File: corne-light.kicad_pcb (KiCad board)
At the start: 2 copper layers, 279.5 x 91.4 mm, 112 parts, among them J1 MJ-4PP-9, J2 OLED, J3 Conn_01x02, J4 Conn_01x02, J6 MJ-4PP-9, J7 OLED, SW1 SW_PUSH, SW10 SW_PUSH, SW11 SW_PUSH, SW12 SW_PUSH, SW13 SW_PUSH, SW14 SW_PUSH, SW15 SW_PUSH, SW16 SW_PUSH, SW17 SW_PUSH, SW18 SW_PUSH, SW19 SW_PUSH, SW2 SW_PUSH, SW20 SW_PUSH, SW21 SW_PUSH, SW22 SW_PUSH, SW23 SW_PUSH, SW24 SW_PUSH, SW25 SW_PUSH, SW26 SW_PUSH, SW27 SW_PUSH, SW28 SW_PUSH, SW29 SW_PUSH, SW3 SW_PUSH, SW30 SW_PUSH, SW31 SW_PUSH, SW32 SW_PUSH, SW33 SW_PUSH, SW34 SW_PUSH, SW35 SW_PUSH, SW36 SW_PUSH, SW37 SW_PUSH, SW38 SW_PUSH, SW39 SW_PUSH, SW4 SW_PUSH, SW40 SW_PUSH, SW41 SW_PUSH, SW42 SW_PUSH, SW44 SW_Slide_DPDT, SW45 SW_Slide_DPDT, SW5 SW_PUSH, SW6 SW_PUSH, SW7 SW_PUSH, SW8 SW_PUSH, SW9 SW_PUSH, U1 nice_nano, U2 nice_nano

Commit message: swap stupid trrs for usb-c
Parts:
- removed J1, J6: MJ-4PP-9, kbd:MJ-4PP-9
- added J5: USB_C_Receptacle_USB2.0_16P, Connector_USB:USB_C_Receptacle_XKB_U262-16XN-4BVC11, F.Cu at (19.6, 108.0)
- added J9: USB_C_Receptacle_USB2.0_16P, Connector_USB:USB_C_Receptacle_XKB_U262-16XN-4BVC11, F.Cu at (283.6, 108.0)
- added RSW1: SW_PUSH, Button_Switch_THT:SW_PUSH_1P1T_6x3.5mm_H4.3_APEM_MJTP1243, F.Cu at (274.2, 104.8)
- added RSW2: SW_PUSH, Button_Switch_THT:SW_PUSH_1P1T_6x3.5mm_H4.3_APEM_MJTP1243, F.Cu at (29.0, 104.8)
- J3: moved to B.Cu
- moved SW45 77.7 mm to (273.5, 66.3), turned to 0 degrees
- moved J3 68.9 mm to (228.2, 71.6), turned to 90 degrees
- moved SW44 56.2 mm to (24.8, 66.5), turned to 0 degrees
- moved D13 11.3 mm to (168.8, 107.4)
- moved D1 11.1 mm to (169.0, 69.4)
- moved D7 11.1 mm to (169.0, 88.4)
- moved D10 10.8 mm to (210.3, 83.4)
- moved D15 10.8 mm to (207.3, 102.4)
- moved D16 10.8 mm to (210.3, 102.4)
- moved D19 10.8 mm to (219.6, 122.4)
- moved D20 10.8 mm to (235.8, 122.4)
- moved D21 10.8 mm to (238.8, 122.4)
- moved D3 10.8 mm to (207.3, 64.4)
- moved D4 10.8 mm to (210.3, 64.4)
- moved D9 10.8 mm to (207.3, 83.4)
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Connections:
- J3 pad 1: bat- -> bat+
- J3 pad 2: bat+ -> bat-
- J4 pad 1: bat-_r -> bat+_r
- J4 pad 2: bat+_r -> bat-_r
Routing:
- net Net-(SW44-A-Pad1): track 89.4 -> 5.19 mm
- net bat-: track 0.00 -> 63.1 mm
- net bat+_r: track 113.2 -> 56.7 mm, vias 1 -> 0
- net data: track 0.00 -> 55.5 mm
- net bat+: track 0.00 -> 52.8 mm
- net data_r: track 0.00 -> 52.2 mm
- net reset: track 0.00 -> 49.9 mm, vias 0 -> 2
- net reset_r: track 0.00 -> 43.3 mm, vias 0 -> 1
- net Net-(D5-A): track 0.00 -> 6.78 mm
- net Net-(SW45-A-Pad1): track 0.00 -> 5.43 mm
- net col0: track 170.1 -> 166.9 mm, vias 1 -> 2
- net bat-_r: track 41.5 -> 44.2 mm
- net VDD: track 37.3 -> 39.7 mm, vias 0 -> 1
- net col0_r: track 174.0 -> 172.1 mm, vias 1 -> 2
- net VCC: track 37.1 -> 38.9 mm, vias 0 -> 1
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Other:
- board size 279.5 x 91.4 mm -> 268.8 x 91.4 mm

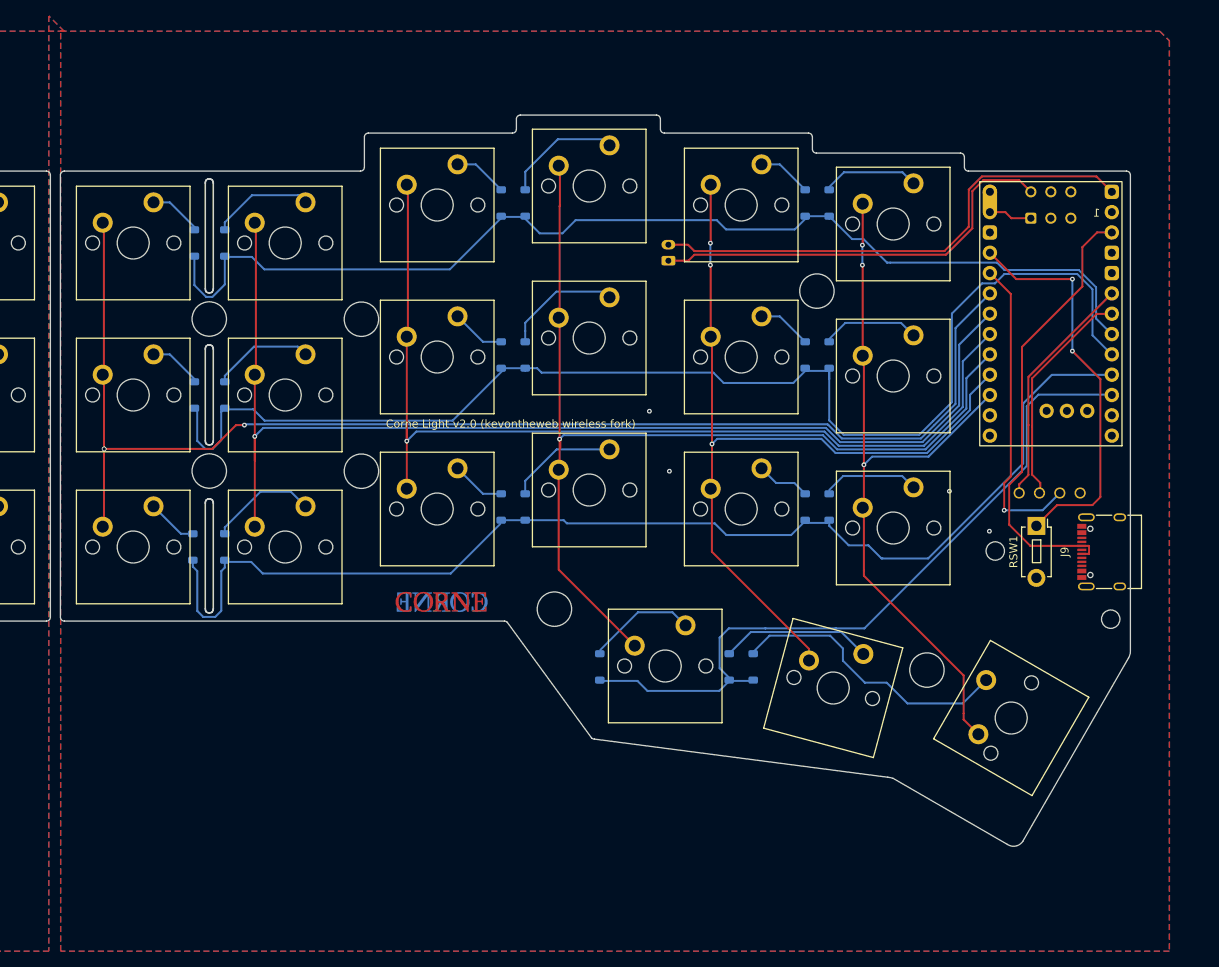
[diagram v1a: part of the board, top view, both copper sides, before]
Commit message: panelised
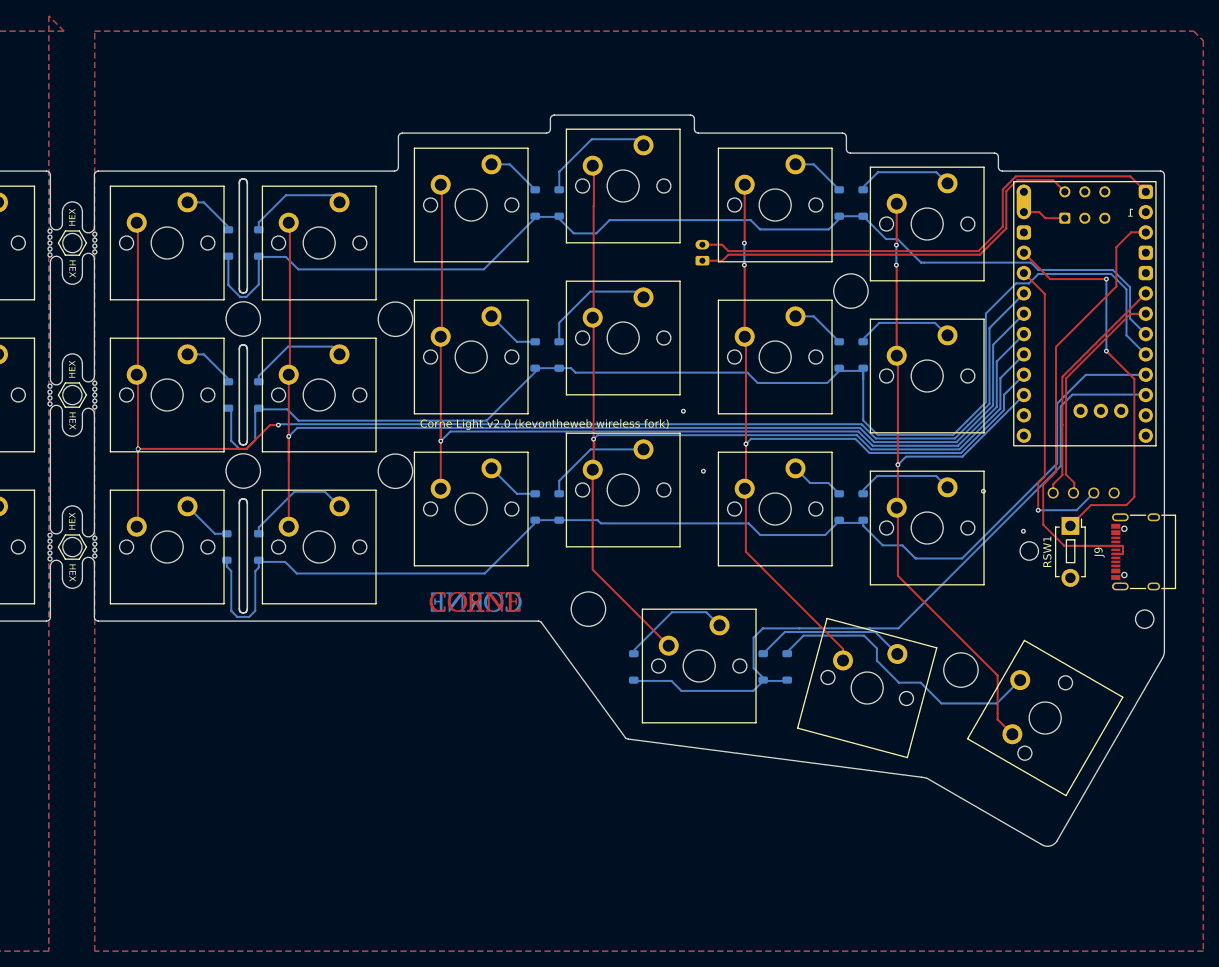
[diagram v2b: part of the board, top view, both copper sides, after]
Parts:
- added MB5: 5.5mm, PCM_marbastlib-various:mousebites_5p5mm_easysnap, F.Cu at (156.5, 69.4)
- added MB5: 5.5mm, PCM_marbastlib-various:mousebites_5p5mm_easysnap, F.Cu at (156.5, 107.4)
- added MB5: 5.5mm, PCM_marbastlib-various:mousebites_5p5mm_easysnap, F.Cu at (151.0, 88.4)
- moved D1 4.25 mm to (173.2, 69.4)
- moved D10 4.25 mm to (214.6, 83.4)
- moved D11 4.25 mm to (249.6, 83.4)
- moved D12 4.25 mm to (252.6, 83.4)
- moved D13 4.25 mm to (173.0, 107.4)
- moved D14 4.25 mm to (177.0, 107.4)
- moved D15 4.25 mm to (211.6, 102.4)
- moved D16 4.25 mm to (214.6, 102.4)
- moved D17 4.25 mm to (249.6, 102.4)
- moved D18 4.25 mm to (252.6, 102.4)
- moved D19 4.25 mm to (223.9, 122.4)
- moved D2 4.25 mm to (177.0, 69.4)
- moved D20 4.25 mm to (240.1, 122.4)
- moved D21 4.25 mm to (243.1, 122.4)
- moved D3 4.25 mm to (211.6, 64.4)
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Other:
- board size 268.8 x 91.4 mm -> 273 x 91.4 mm

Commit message: put jacks back, erc and drc. finishing touches
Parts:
- removed J5, J9: USB_C_Receptacle_USB2.0_16P, Connector_USB:USB_C_Receptacle_XKB_U262-16XN-4BVC11
- removed SW45: SW_Slide_DPDT, Button_Switch_THT:SW_CK_JS202011AQN_DPDT_Angled
- added J6: AudioJack4, custom:PJ320A, F.Cu at (286.7, 110.3)
- added J8: AudioJack4, custom:PJ320A, F.Cu at (20.7, 105.7)
- added SW46: SW_SPDT, custom:MSK-12C01-07(1P2T), B.Cu at (276.4, 62.1)
- SW44: value SW_Slide_DPDT -> SW_SPDT; footprint Button_Switch_THT:SW_CK_JS202011AQN_DPDT_Angled -> custom:MSK-12C01-07(1P2T)
- moved RSW2 10.3 mm to (29.4, 115.1), turned to 180 degrees
- moved RSW1 10.1 mm to (278.1, 114.9), turned to 0 degrees
- moved SW44 4.40 mm to (23.4, 62.3), turned to -90 degrees
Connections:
- SW44 pad 1: Net-(SW44-A-Pad1) -> unconnected-(SW44-A-Pad1)
- SW44 pad 2: unconnected-(SW44-B-Pad2) -> Net-(SW44-B)
- SW44 pad 3: unconnected-(SW44-C-Pad3) -> bat+_r
- U2 pad 13: Net-(SW44-A-Pad1) -> Net-(SW44-B)
- U2 pad 29: Net-(SW44-A-Pad1) -> Net-(SW44-B)
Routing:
- net reset_r: track 43.3 -> 55.6 mm
- net VCC: track 38.9 -> 49.5 mm
- net reset: track 49.9 -> 59.9 mm, vias 2 -> 3
- net Net-(SW44-B): track 0.00 -> 9.30 mm
- net bat+: track 52.8 -> 60.7 mm, vias 0 -> 1
- net Net-(SW44-A-Pad1): track 5.19 -> 0.00 mm
- net data: track 55.5 -> 50.6 mm
- net Net-(SW46-B): track 5.43 -> 9.86 mm
- net bat+_r: track 56.7 -> 53.9 mm
- net data_r: track 52.2 -> 49.6 mm, vias 0 -> 1
- net VDD: track 39.7 -> 42.2 mm
- net row0: track 138.0 -> 139.0 mm
- net row2_r: track 132.6 -> 131.6 mm
- net bat-: track 63.1 -> 62.4 mm
- net SDA_r: track 30.2 -> 29.5 mm
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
